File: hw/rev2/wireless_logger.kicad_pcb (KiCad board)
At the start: 4 copper layers, 144 parts, among them J1 FCI 10118194, J2 CONN_2, J3 SSD1306_SER, J4 SWD_10PIN, J5 CONN_5, P1 CONN_6X2, Q1 2N7002P, Q2 2N7002P, U1 MT29FXX01A, U10 CC2541, U11 STM32F40X_BGA176, U2 MAG3110, U3 MMA8452Q, U4 LPS331AP, U5 L3GD20, U6 MCP111T-315, U7 BQ24095, U8 TPS62698, U9 CC1101, X1 FA-128 26.0000MF10Z-W3, X2 9HT10-32.768KBZF-T, X3 FA-128 32.0000MF20X-K3, X4 XRCGB25M000F0L00R0, X5 9HT10-32.768KBZF-T

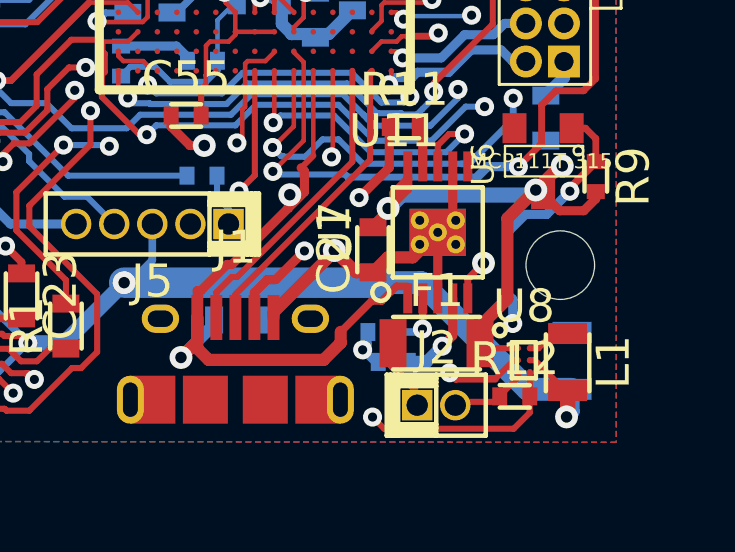
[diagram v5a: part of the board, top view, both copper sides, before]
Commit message: Fixed huge problem with regulator footprint pin layout
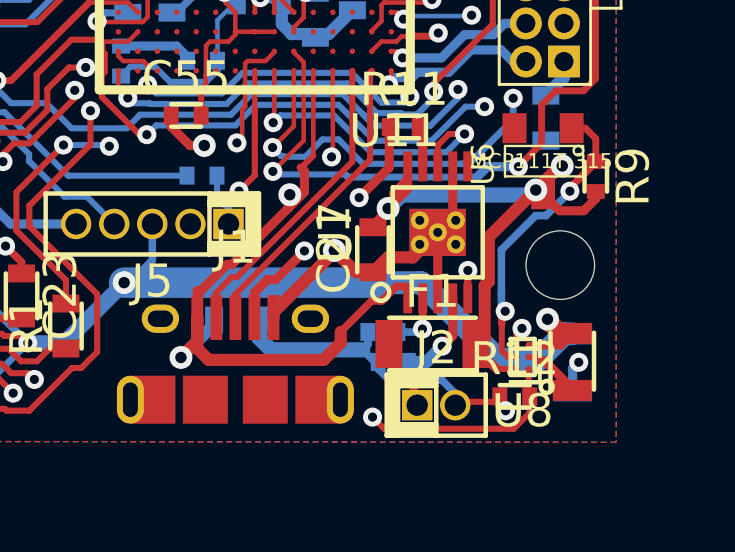
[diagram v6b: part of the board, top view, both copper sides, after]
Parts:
- moved L1 0.16 mm to (198.5, 157.3), turned to 90 degrees
- moved F1 0.14 mm to (193.9, 156.7)
- moved U8 0.12 mm to (196.9, 157.2), turned to 180 degrees
- moved C22 0.05 mm to (198.6, 157.3), turned to 90 degrees
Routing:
- net GND: track 257.7 -> 266.6 mm, vias 54 -> 56
- net N-00000193: track 14.2 -> 10.3 mm, vias 3 -> 2
- net V3: track 311.1 -> 308.6 mm
- net N-00000194: track 2.50 -> 1.50 mm
- net Vbat: track 91.2 -> 91.8 mm
- net /STM32F4/REG_nUSB_CONN: track 16.9 -> 17.5 mm

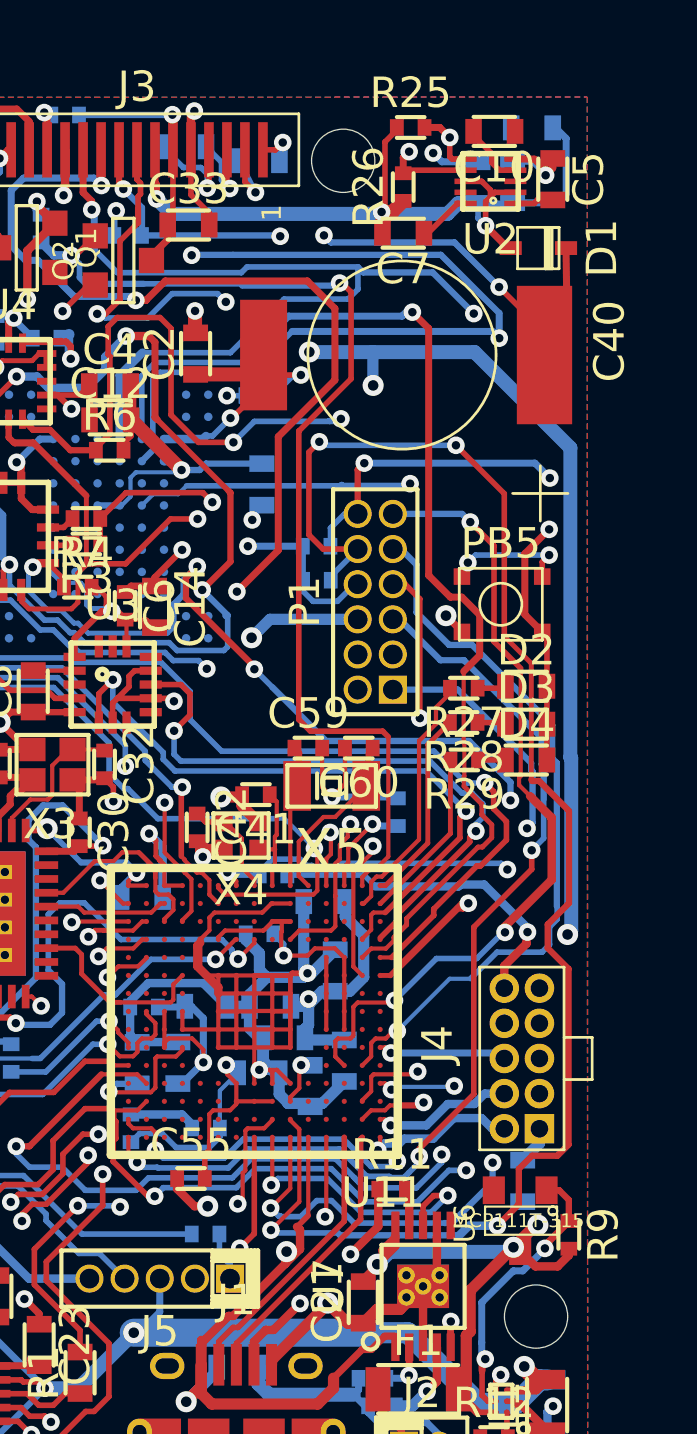
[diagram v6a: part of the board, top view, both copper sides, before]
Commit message: Added pullup to flash nCS
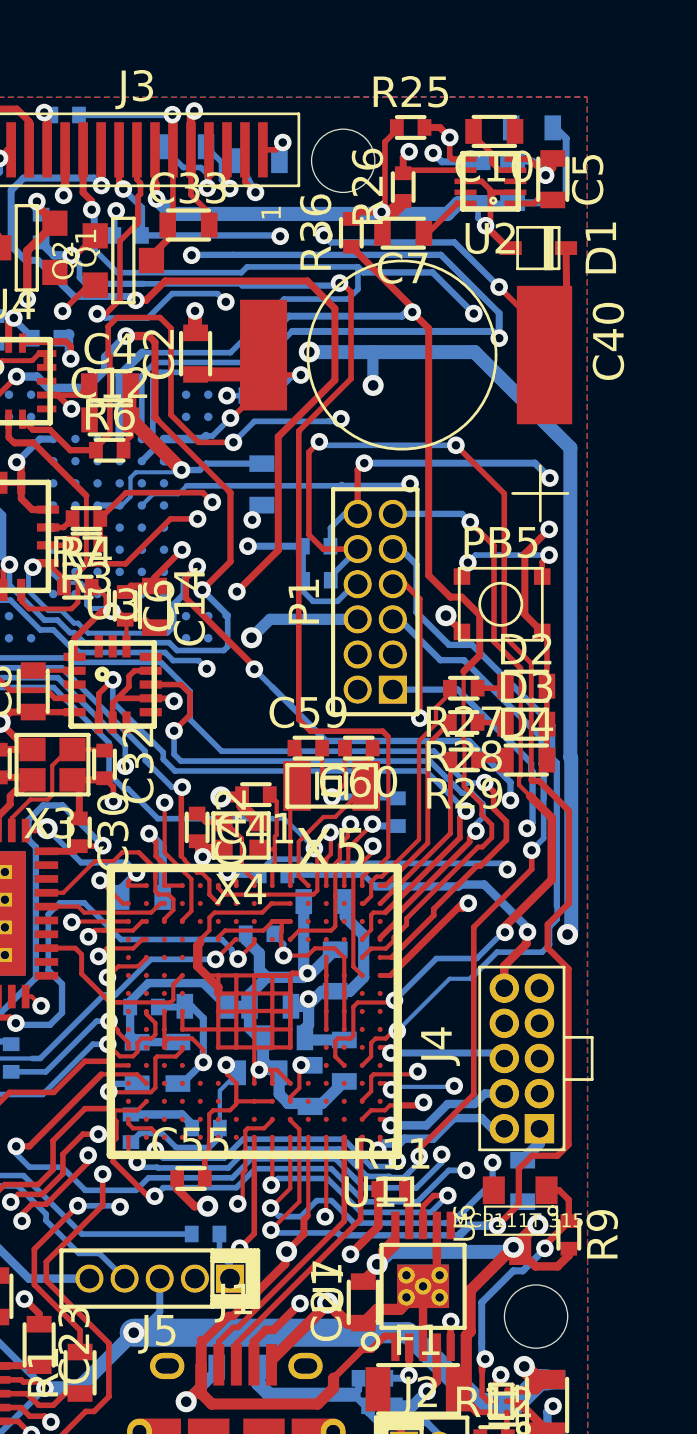
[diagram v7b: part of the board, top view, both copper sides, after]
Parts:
- added R36: 100k, SMD0402, F.Cu at (191.5, 114.9)
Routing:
- net /STM32F4/FLASH_nCS: track 40.7 -> 44.0 mm
- net V3: track 308.6 -> 310.0 mm
- net Vbus: track 53.4 -> 52.8 mm
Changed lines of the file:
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@@
 (kicad_pcb (version 3) (host pcbnew "(2013-mar-30)-stable")
   (general
-    (links 473)
+    (links 475)
     (no_connects 0)
     (area 0 0 0 0)
     (thickness 1.6)
     (drawings 4)
-    (tracks 2776)
+    (tracks 2779)
     (zones 0)
-    (modules 144)
+    (modules 145)
     (nets 114)
   )
@@
   (net 97 N-00000237)
   (net 98 N-00000238)
-  (net 99 N-0000042)
-  (net 100 N-0000043)
-  (net 101 N-0000044)
-  (net 102 N-0000045)
+  (net 99 N-0000041)
+  (net 100 N-0000042)
+  (net 101 N-0000043)
+  (net 102 N-0000044)
   (net 103 N-0000063)
   (net 104 N-0000064)
@@
     (add_net N-00000237)
     (add_net N-00000238)
+    (add_net N-0000041)
     (add_net N-0000042)
     (add_net N-0000043)
     (add_net N-0000044)
-    (add_net N-0000045)
     (add_net N-0000063)
     (add_net N-0000064)
@@
     (pad 1 smd rect (at -1.69926 -2.10058 180) (size 1.00076 1.30048)
       (layers F.Cu F.Paste F.Mask)
-      (net 102 N-0000045)
+      (net 102 N-0000044)
     )
     (pad 1 smd rect (at -1.7018 2.10058 180) (size 1.00076 1.30048)
       (layers F.Cu F.Paste F.Mask)
-      (net 102 N-0000045)
+      (net 102 N-0000044)
     )
     (pad 2 smd rect (at 1.69926 2.10058 180) (size 1.00076 1.30048)
@@
     (pad 1 smd rect (at -1.69926 -2.10058 180) (size 1.00076 1.30048)
       (layers F.Cu F.Paste F.Mask)
-      (net 101 N-0000044)
+      (net 101 N-0000043)
     )
     (pad 1 smd rect (at -1.7018 2.10058 180) (size 1.00076 1.30048)
       (layers F.Cu F.Paste F.Mask)
-      (net 101 N-0000044)
+      (net 101 N-0000043)
     )
     (pad 2 smd rect (at 1.69926 2.10058 180) (size 1.00076 1.30048)
@@
     (pad 1 smd rect (at -1.69926 -2.10058 180) (size 1.00076 1.30048)
       (layers F.Cu F.Paste F.Mask)
-      (net 100 N-0000043)
+      (net 100 N-0000042)
     )
     (pad 1 smd rect (at -1.7018 2.10058 180) (size 1.00076 1.30048)
       (layers F.Cu F.Paste F.Mask)
-      (net 100 N-0000043)
+      (net 100 N-0000042)
     )
     (pad 2 smd rect (at 1.69926 2.10058 180) (size 1.00076 1.30048)
@@
     (pad 1 smd rect (at -1.69926 -2.10058 180) (size 1.00076 1.30048)
       (layers F.Cu F.Paste F.Mask)
-      (net 99 N-0000042)
+      (net 99 N-0000041)
     )
     (pad 1 smd rect (at -1.7018 2.10058 180) (size 1.00076 1.30048)
       (layers F.Cu F.Paste F.Mask)
-      (net 99 N-0000042)
+      (net 99 N-0000041)
     )
     (pad 2 smd rect (at 1.69926 2.10058 180) (size 1.00076 1.30048)
@@
     (pad 1 smd rect (at -0.5 0 270) (size 0.5 0.6)
       (layers B.Cu B.Paste B.Mask)
-      (net 102 N-0000045)
+      (net 102 N-0000044)
     )
   )
@@
     (pad 1 smd rect (at -0.5 0 270) (size 0.5 0.6)
       (layers B.Cu B.Paste B.Mask)
-      (net 99 N-0000042)
+      (net 99 N-0000041)
     )
   )
@@
     (pad 1 smd rect (at -0.5 0 270) (size 0.5 0.6)
       (layers B.Cu B.Paste B.Mask)
-      (net 100 N-0000043)
+      (net 100 N-0000042)
     )
   )
@@
     (pad 1 smd rect (at -0.5 0 270) (size 0.5 0.6)
       (layers B.Cu B.Paste B.Mask)
-      (net 101 N-0000044)
+      (net 101 N-0000043)
     )
   )
@@
     )
   )
+  (module SMD0402 (layer F.Cu)
+    (at 191.4652 114.935 90)
+    (descr "0402 SMD for reflow")
+    (fp_text reference R36 (at 0 -1.25 90) (layer F.SilkS)
+      (effects (font (size 1.1 1.1) (thickness 0.17)))
+    )
+    (fp_text value 100k (at 0 1.375 90) (layer F.SilkS) hide
+      (effects (font (size 1.1 1.1) (thickness 0.17)))
+    )
+    (fp_line (start -0.5 0.375) (end 0.5 0.375) (layer F.SilkS) (width 0.15))
+    (fp_line (start -0.5 -0.375) (end 0.5 -0.375) (layer F.SilkS) (width 0.15))
+    (pad 2 smd rect (at 0.5 0 90) (size 0.5 0.6)
+      (layers F.Cu F.Paste F.Mask)
+      (net 111 V3)
+    )
+    (pad 1 smd rect (at -0.5 0 90) (size 0.5 0.6)
+      (layers F.Cu F.Paste F.Mask)
+      (net 25 /STM32F4/FLASH_nCS)
+    )
+  )
   (gr_line (start 170 160) (end 170 110) (angle 90) (layer Cmts.User) (width 0.2))
   (gr_line (start 200 160) (end 170 160) (angle 90) (layer Cmts.User) (width 0.2))
@@
   (segment (start 176.21504 146.97964) (end 177.3682 146.97964) (width 0.2032) (layer B.Cu) (net 24))
   (segment (start 176.1744 147.02028) (end 176.21504 146.97964) (width 0.2032) (layer B.Cu) (net 24))
+  (segment (start 191.4652 115.435) (end 193.66992 117.63972) (width 0.254) (layer F.Cu) (net 25) (status 400000))
+  (segment (start 193.66992 117.63972) (end 193.66992 117.8052) (width 0.254) (layer F.Cu) (net 25))
   (segment (start 184.3786 119.623842) (end 187.518038 119.623842) (width 0.2032) (layer B.Cu) (net 25))
   (segment (start 187.518038 119.623842) (end 187.58916 119.55272) (width 0.2032) (layer B.Cu) (net 25))
@@
   (segment (start 189.63641 131.419884) (end 189.63641 122.14859) (width 0.2032) (layer Inner2.Cu) (net 60))
   (segment (start 189.63641 122.14859) (end 190.08852 121.69648) (width 0.2032) (layer Inner2.Cu) (net 60))
+  (segment (start 197.39356 112.27308) (end 197.90156 112.27308) (width 0.2032) (layer F.Cu) (net 61))
+  (segment (start 197.90156 112.27308) (end 198.48576 112.85728) (width 0.2032) (layer F.Cu) (net 61))
   (segment (start 192.07264 157.3276) (end 192.07264 157.56674) (width 0.254) (layer B.Cu) (net 61))
   (segment (start 194.6402 158.3817) (end 194.6402 158.77032) (width 0.254) (layer B.Cu) (net 61))
@@
   (segment (start 195.30822 113.87582) (end 195.5927 113.87582) (width 0.2032) (layer F.Cu) (net 61) (status 30))
   (segment (start 194.2338 114.95024) (end 195.30822 113.87582) (width 0.2032) (layer F.Cu) (net 61) (status 30))
-  (segment (start 197.39356 112.27308) (end 198.07936 112.27308) (width 0.254) (layer F.Cu) (net 61) (status 10))
-  (segment (start 198.48576 112.67948) (end 198.48576 112.85728) (width 0.254) (layer F.Cu) (net 61))
-  (segment (start 198.07936 112.27308) (end 198.48576 112.67948) (width 0.254) (layer F.Cu) (net 61))
   (segment (start 198.74484 112.24952) (end 198.74484 112.5982) (width 0.254) (layer F.Cu) (net 61) (status 10))
   (segment (start 198.02532 112.35112) (end 197.29196 112.35112) (width 0.254) (layer B.Cu) (net 61) (status 20))
@@
   (segment (start 188.6077 138.52652) (end 188.6077 137.8839) (width 0.1524) (layer F.Cu) (net 110) (status 10))
   (segment (start 188.6077 137.8839) (end 188.70168 137.78992) (width 0.1524) (layer F.Cu) (net 110))
+  (segment (start 191.4652 114.435) (end 191.71704 114.18316) (width 0.254) (layer F.Cu) (net 111) (status 400000))
+  (segment (start 191.71704 114.18316) (end 192.5574 114.18316) (width 0.254) (layer F.Cu) (net 111))
+  (segment (start 196.3166 114.681) (end 196.49186 114.50574) (width 0.2032) (layer F.Cu) (net 111))
+  (segment (start 196.49186 114.50574) (end 196.49186 113.39322) (width 0.2032) (layer F.Cu) (net 111))
   (segment (start 198.5518 156.3903) (end 198.1987 156.3903) (width 0.508) (layer B.Cu) (net 111))
   (segment (start 198.1987 156.3903) (end 197.7136 155.9052) (width 0.508) (layer B.Cu) (net 111))
@@
   (via (at 196.3166 114.681) (size 0.635) (layers F.Cu B.Cu) (net 111))
   (segment (start 196.3166 114.681) (end 196.04228 114.40668) (width 0.2032) (layer B.Cu) (net 111))
-  (segment (start 196.3166 113.80724) (end 196.3166 114.681) (width 0.2032) (layer F.Cu) (net 111))
   (segment (start 196.64934 113.4745) (end 196.49186 113.63198) (width 0.2032) (layer F.Cu) (net 111))
-  (segment (start 196.49186 113.63198) (end 196.3166 113.80724) (width 0.2032) (layer F.Cu) (net 111))
   (segment (start 174.4444 137.28744) (end 174.44256 137.28744) (width 0.254) (layer F.Cu) (net 111) (status 30))
   (segment (start 174.44256 137.28744) (end 173.78172 136.6266) (width 0.254) (layer F.Cu) (net 111) (status 10))
@@
   (segment (start 192.56756 151.69804) (end 193.056 151.2096) (width 0.254) (layer F.Cu) (net 112) (status 20))
   (segment (start 192.56756 152.16816) (end 192.56756 151.69804) (width 0.254) (layer F.Cu) (net 112))
+  (segment (start 189.12332 151.75484) (end 189.7507 151.12746) (width 0.254) (layer F.Cu) (net 113))
+  (segment (start 189.7507 151.12746) (end 189.7507 150.6093) (width 0.254) (layer F.Cu) (net 113))
+  (segment (start 189.8523 150.5077) (end 189.7507 150.6093) (width 0.2286) (layer F.Cu) (net 113))
+  (segment (start 189.90818 150.45182) (end 189.8523 150.5077) (width 0.2032) (layer F.Cu) (net 113))
+  (segment (start 189.90818 147.6248) (end 189.90818 150.45182) (width 0.1524) (layer F.Cu) (net 113) (status 10))
   (segment (start 186.76112 132.0038) (end 187.0964 131.66852) (width 0.4064) (layer Inner2.Cu) (net 113))
   (segment (start 186.76112 134.01548) (end 186.76112 132.0038) (width 0.4064) (layer Inner2.Cu) (net 113))
@@
   (segment (start 186.16168 154.95016) (end 187.033069 154.078771) (width 0.3048) (layer F.Cu) (net 113))
   (segment (start 187.033069 154.078771) (end 187.195291 154.078771) (width 0.3048) (layer F.Cu) (net 113))
-  (segment (start 189.611 150.96744) (end 189.50178 150.85822) (width 0.3048) (layer F.Cu) (net 113))
-  (segment (start 189.611 151.663062) (end 189.611 150.96744) (width 0.3048) (layer F.Cu) (net 113))
-  (segment (start 189.074891 152.199171) (end 189.611 151.663062) (width 0.3048) (layer F.Cu) (net 113))
-  (segment (start 189.90818 147.6248) (end 189.90818 150.45182) (width 0.1524) (layer F.Cu) (net 113) (status 10))
-  (segment (start 189.90818 150.45182) (end 189.50178 150.85822) (width 0.2032) (layer F.Cu) (net 113))
   (segment (start 186.6004 155.64796) (end 186.6004 155.9306) (width 0.2032) (layer B.Cu) (net 113) (status 30))
   (segment (start 193.056 154.8096) (end 192.67256 154.8096) (width 0.254) (layer F.Cu) (net 113) (status 10))

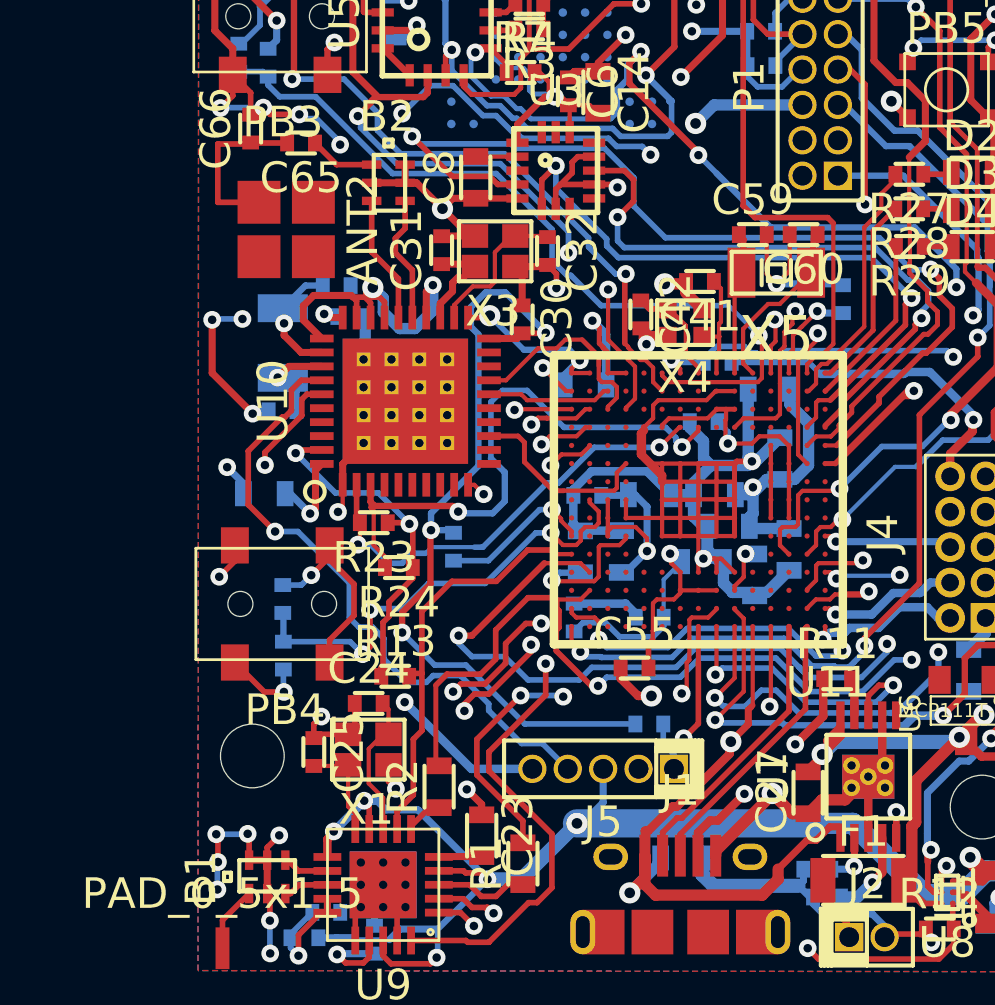
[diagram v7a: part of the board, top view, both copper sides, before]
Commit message: Added some extra decoupling caps for bluetooth
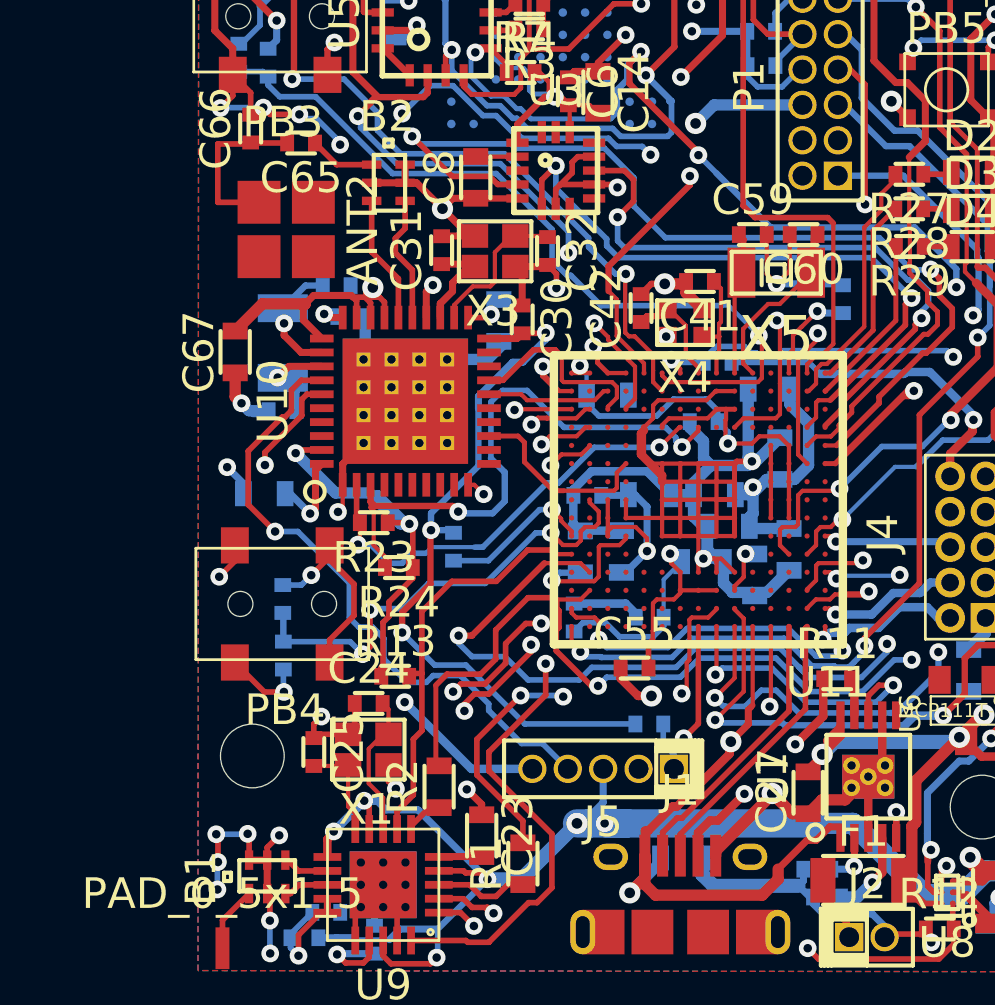
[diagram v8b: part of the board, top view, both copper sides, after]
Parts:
- added C67: 1u, SMD0603, F.Cu at (171.3, 137.8)
- added C68: 1u, SMD0603, B.Cu at (180.8, 136.6)
- moved C47 0.88 mm to (184.7, 139.3)
- moved C42 0.23 mm to (185.9, 136.2), turned to 90 degrees
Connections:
- U11 pad D1: /STM32F4/OLED_nCS -> (no net)
- U11 pad L1: (no net) -> /STM32F4/OLED_nCS
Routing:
- net V3: track 310.0 -> 321.9 mm, vias 28 -> 29
- net GND: track 266.5 -> 262.2 mm, vias 56 -> 54
- net /Bluetooth/RF_RESET_N_LOCAL: track 29.1 -> 25.8 mm
- net /STM32F4/OLED_nRES: track 39.5 -> 38.5 mm
